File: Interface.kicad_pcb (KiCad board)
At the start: 4 copper layers, 126.8 x 95.1 mm, 92 parts, among them J101 AudioJack4, J102 switch, J3 TYPE-C-31-M-12, J4 CONN_DISPLAY, Q1 2N7002VC-7, Q2 2N7002VC-7, U1 W25Q128JVPIQ, U2 RP2040, U3 XC6210B332MR-G, Y1 12MHz

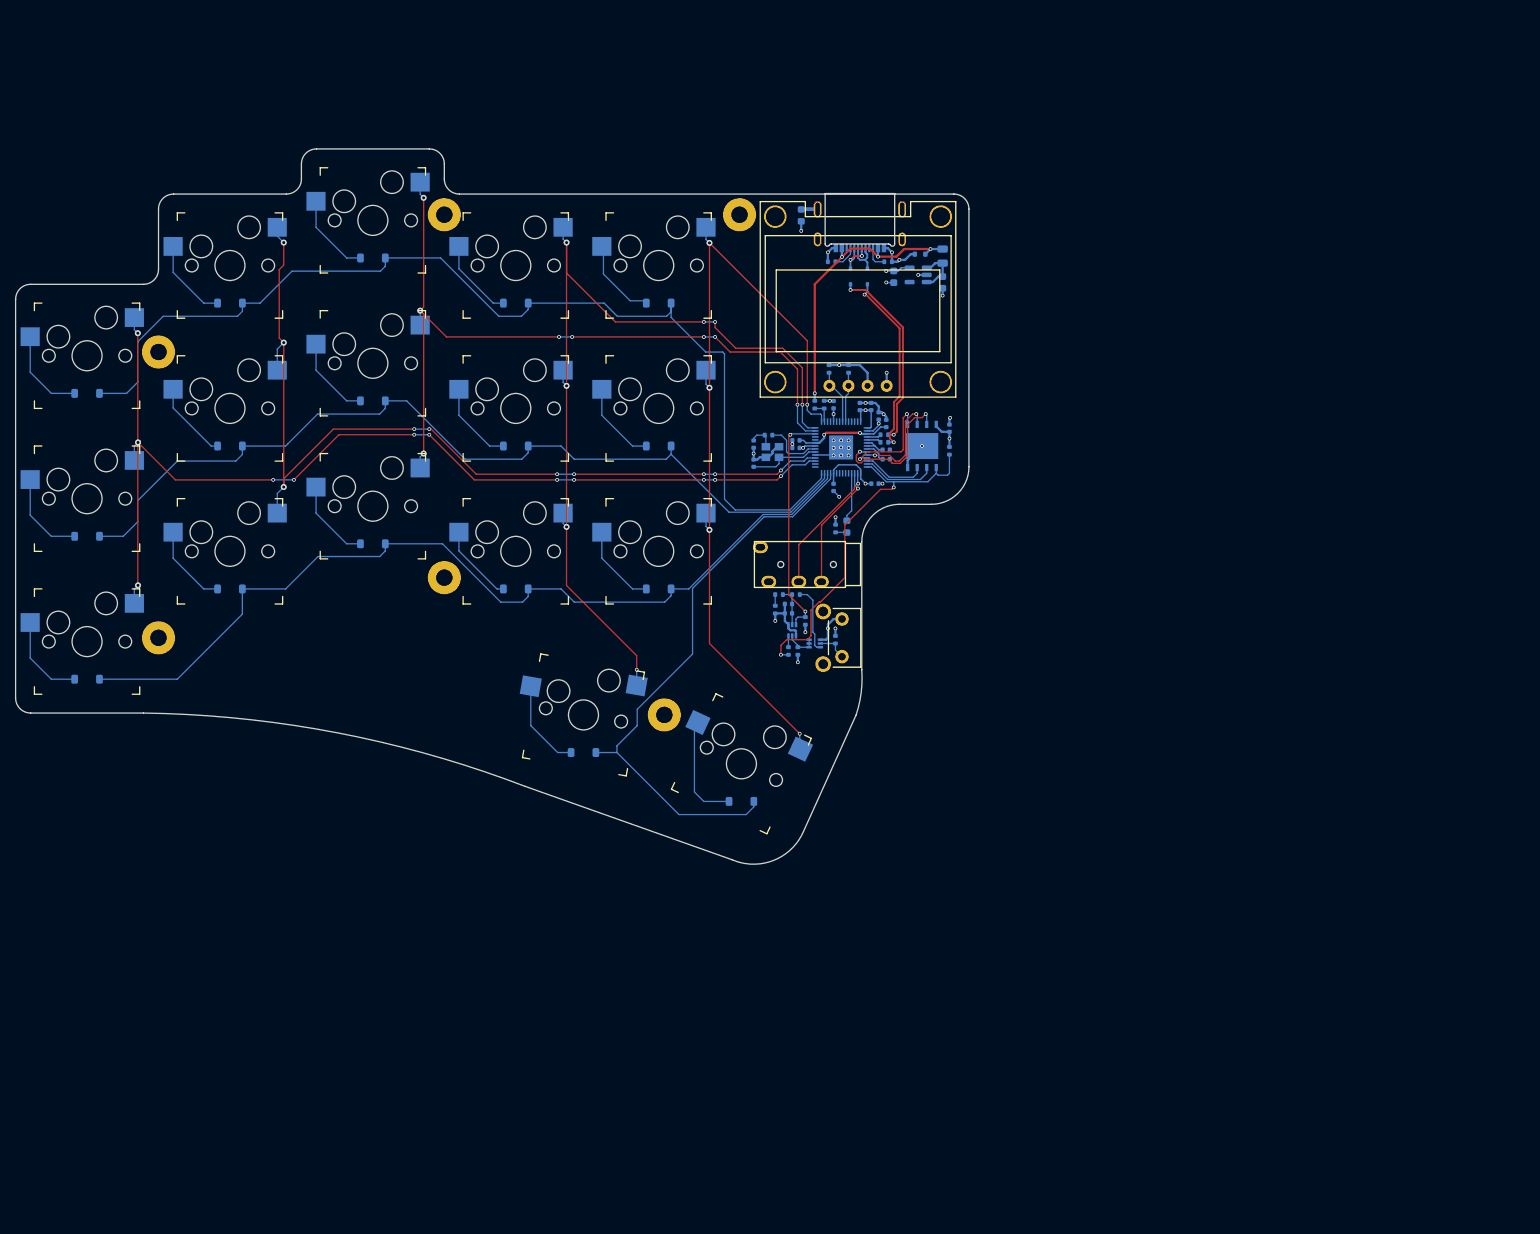
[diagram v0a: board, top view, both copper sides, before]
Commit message: Rotate and add mirror line
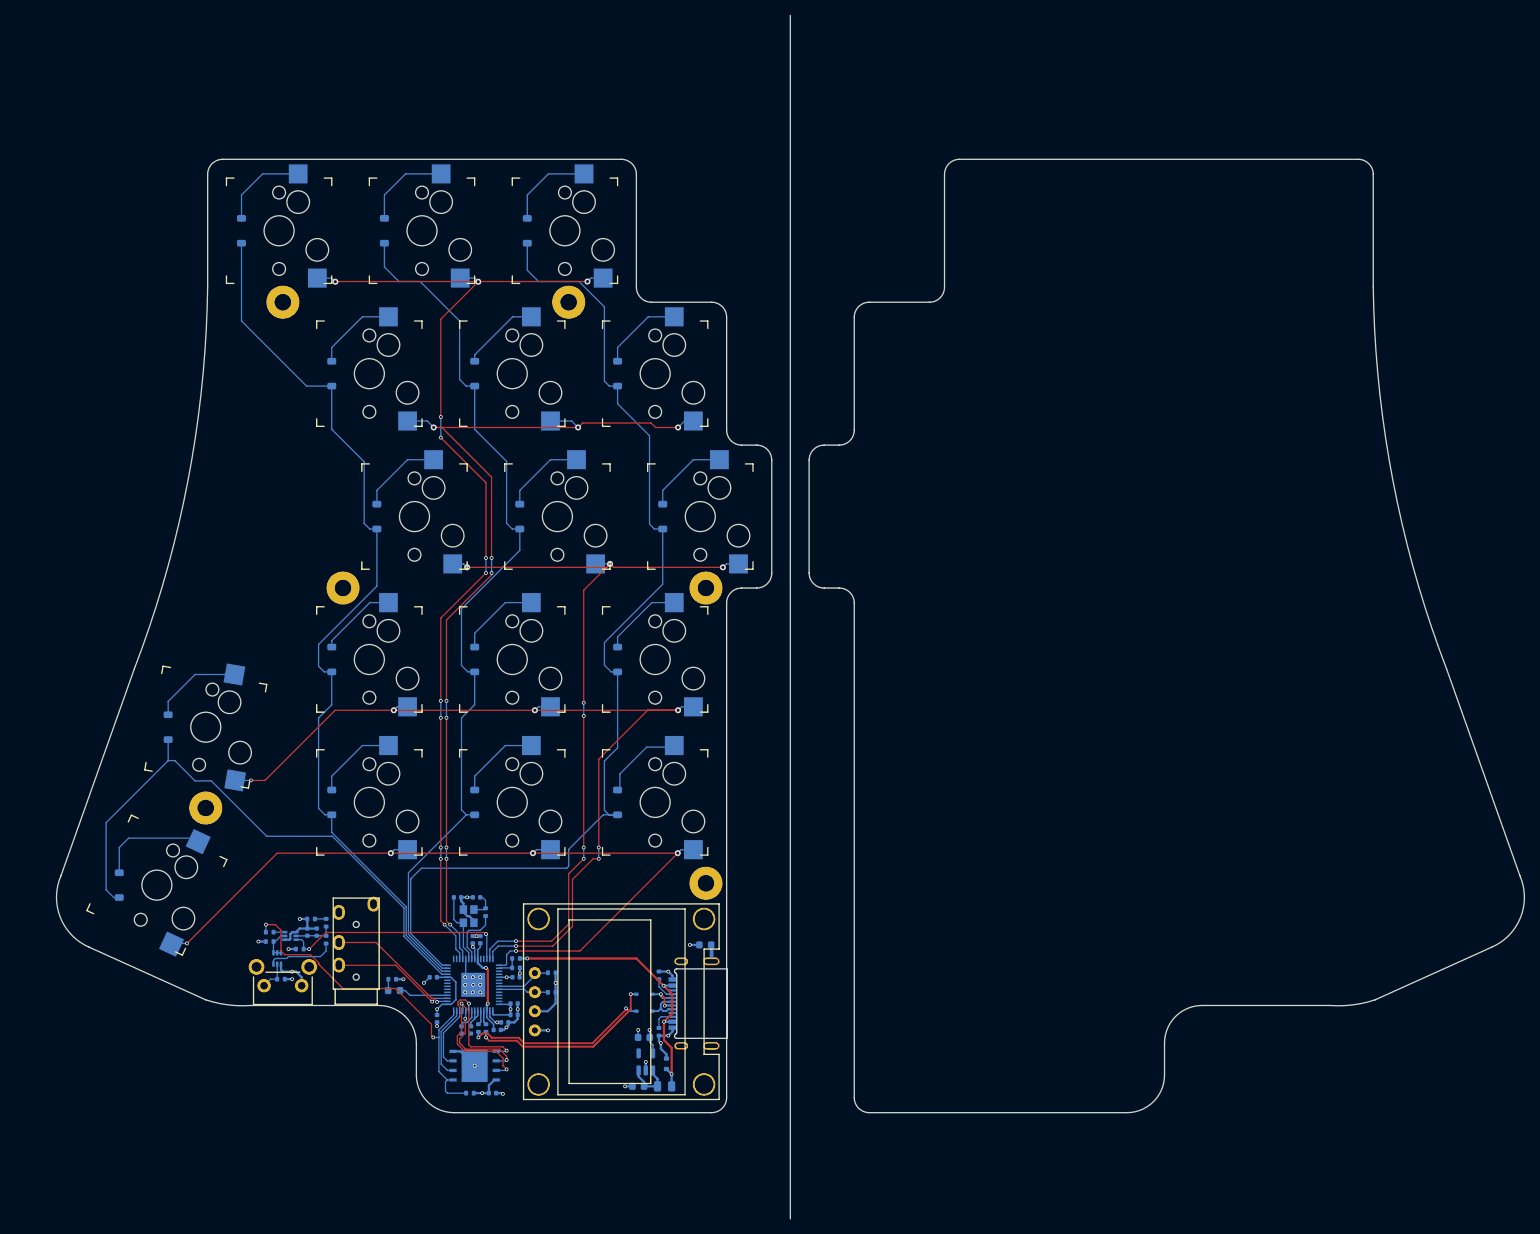
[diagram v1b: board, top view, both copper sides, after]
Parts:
- moved F1 116.4 mm to (108.5, 157.4), turned to 180 degrees
- moved C15 114.3 mm to (105.0, 157.4), turned to 180 degrees
- moved D2 112.8 mm to (108.8, 154.4), turned to 90 degrees
- moved U3 110.7 mm to (106.0, 154.1), turned to 90 degrees
- moved J3 107.4 mm to (114.8, 146.4), turned to -90 degrees
- moved C1 107.3 mm to (85.7, 158.3), turned to 0 degrees
- moved R10 106.8 mm to (107.8, 150.1), turned to -90 degrees
- moved R2 106.6 mm to (82.7, 158.3), turned to 180 degrees
- moved C16 106.4 mm to (105.8, 150.9), turned to 180 degrees
- moved D4 102.1 mm to (105.8, 147.4), turned to 180 degrees
- moved U1 101.6 mm to (83.3, 154.6), turned to 0 degrees
- moved D3 99.3 mm to (105.8, 145.1), turned to 180 degrees
- moved J4 98.5 mm to (102.8, 146.1), turned to 90 degrees
- moved FB1 97.8 mm to (113.9, 138.6), turned to 180 degrees
- moved R9 97.6 mm to (107.8, 142.6), turned to -90 degrees
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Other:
- board size 126.8 x 95.1 mm -> 195.2 x 160 mm
